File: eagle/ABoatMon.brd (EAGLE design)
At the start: 78.7 x 61 mm, 29 parts, among them J1 5V, J2 GND, J3 GND, J4 5V, X1 MKDSN1,5/2-5,08

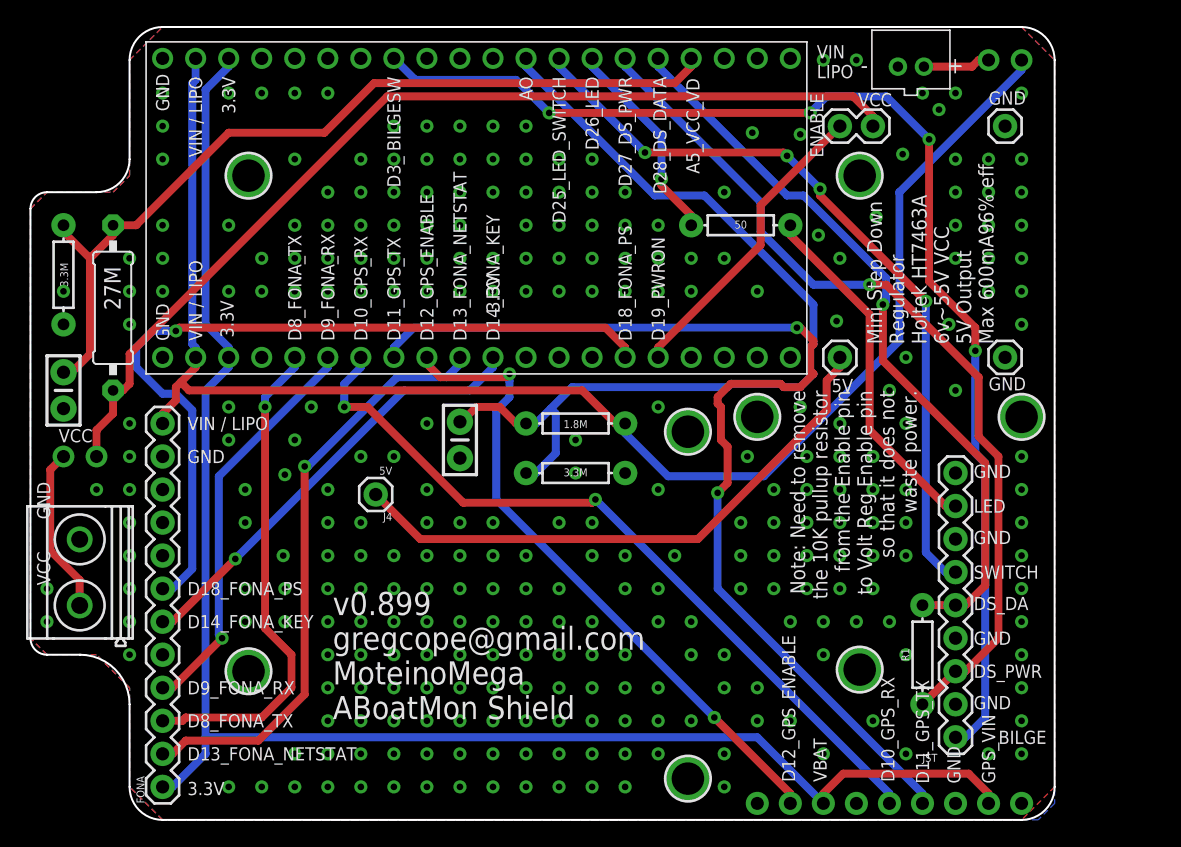
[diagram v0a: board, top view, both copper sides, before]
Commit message: moved 9 pin jst
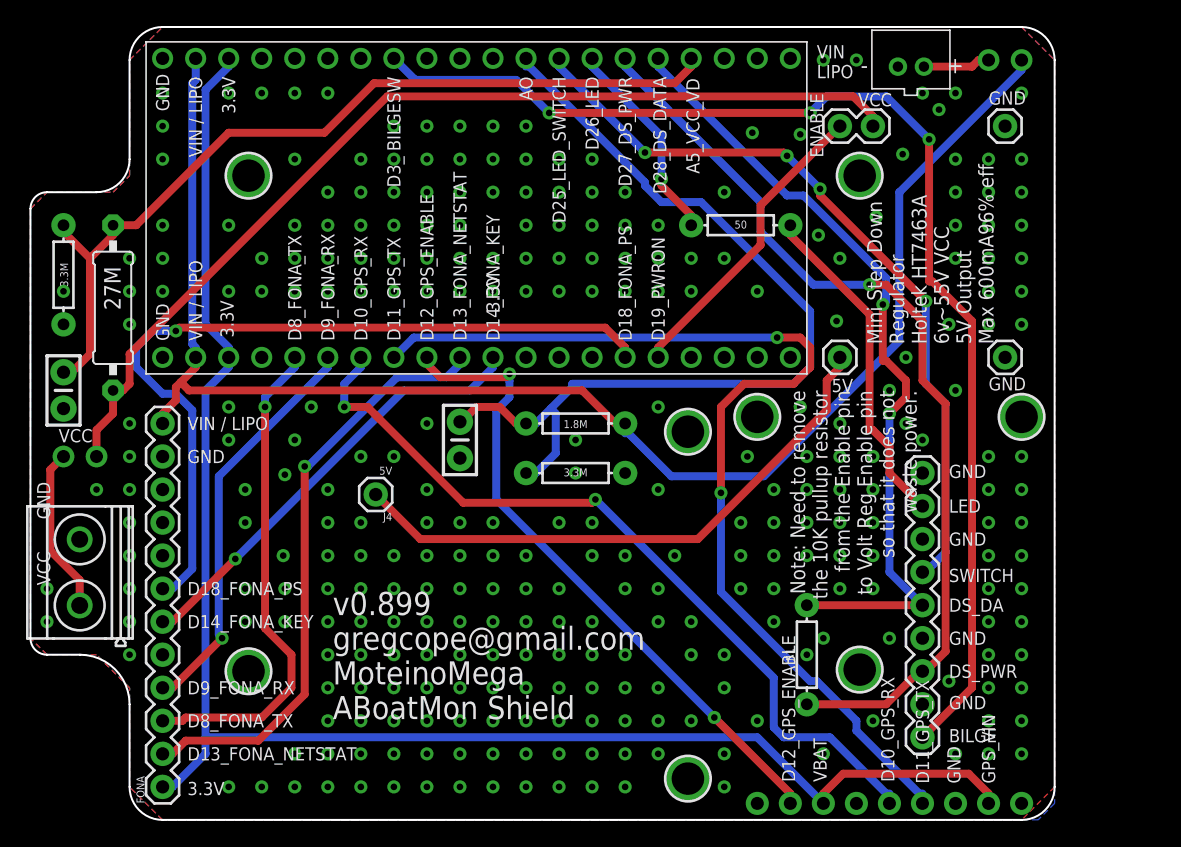
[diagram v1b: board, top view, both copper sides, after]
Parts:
- moved R1 8.89 mm to (61.0, 12.7)
- moved JST 2.54 mm to (69.8, 6.35)
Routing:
- net D28_DS_DATA: track 57.3 -> 61.5 mm, vias 1 -> 2
- net D27_DS_PWR: track 67.7 -> 71.4 mm
- net D11_GPS_TX: track 83.5 -> 80.5 mm
- net D10_GPS_RX: track 59.5 -> 62.3 mm
- net LED: track 27.3 -> 25.9 mm
- net A0: track 72.4 -> 71.6 mm
- net VIN: track 117.8 -> 118.4 mm
- net D3_BILGESW: track 93.9 -> 93.8 mm, vias 4 -> 3

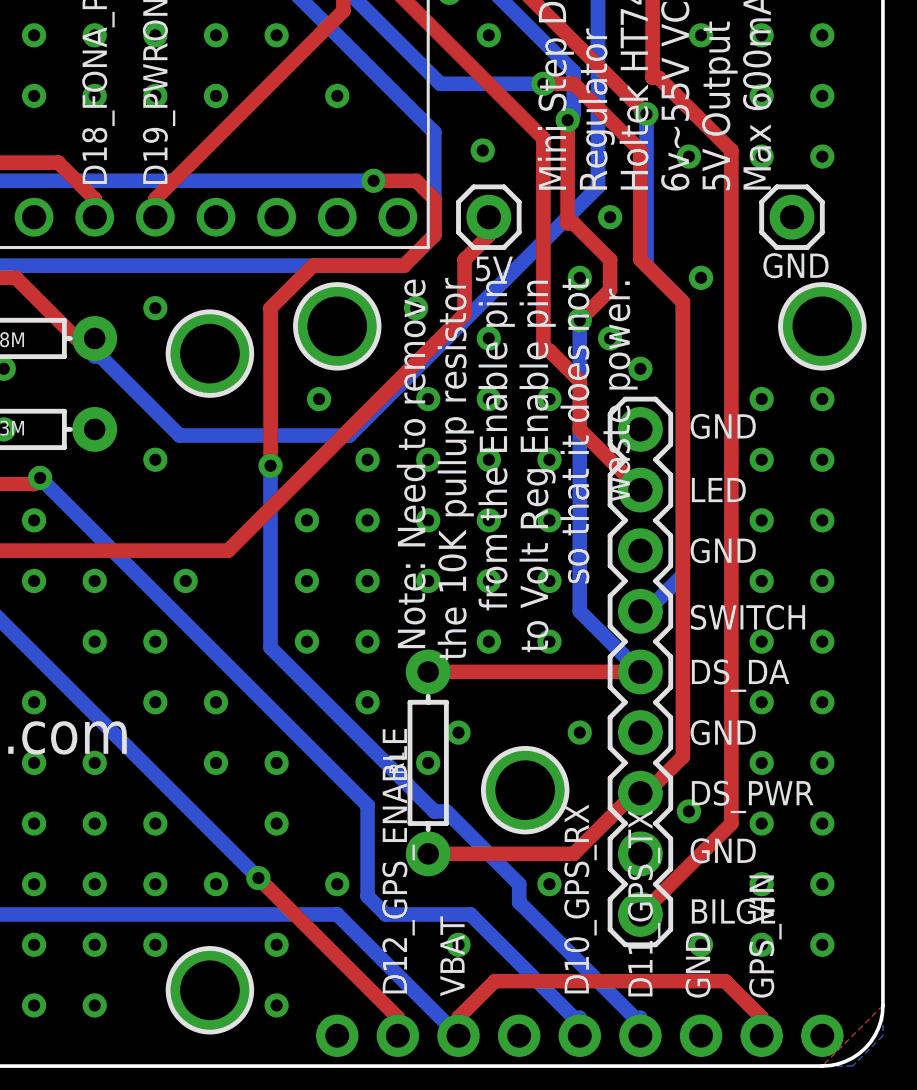
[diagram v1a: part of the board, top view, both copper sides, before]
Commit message: moved large JST
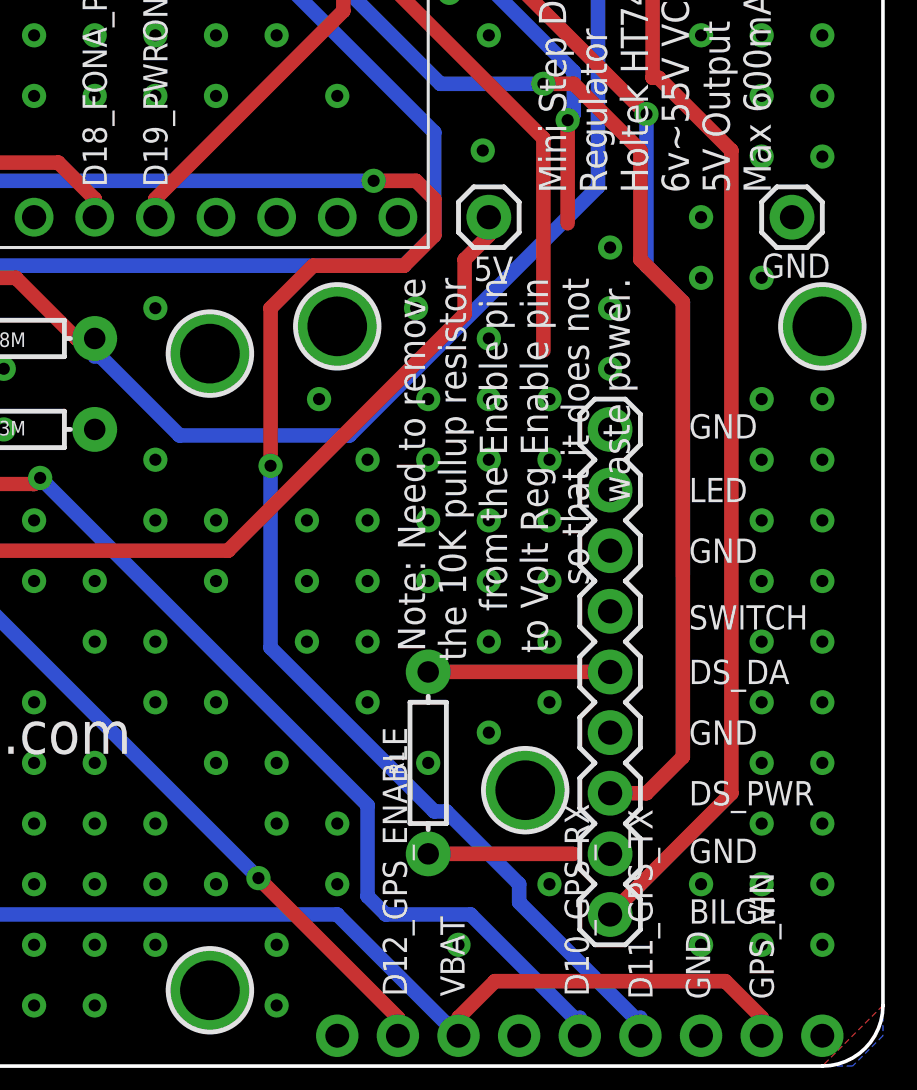
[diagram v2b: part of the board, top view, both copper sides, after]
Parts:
- moved JST 1.27 mm to (68.6, 6.35)
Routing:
- net D28_DS_DATA: track 61.5 -> 39.0 mm, vias 2 -> 1
- net LED: track 25.9 -> 18.3 mm
- net D27_DS_PWR: track 71.4 -> 68.8 mm
- net D25_LED_SWITCH: track 59.3 -> 56.9 mm
- net D3_BILGESW: track 93.8 -> 94.4 mm

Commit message: message logic
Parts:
- added J5: (no value), SparkFun-Connectors:JST-4-PTH
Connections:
- new net D16_SCL: J5.3, MOTEINO_MEGA.D16
- new net D17_SDA: J5.4, MOTEINO_MEGA.D17
- new net D20_OLED_VCC: J5.2, MOTEINO_MEGA.D20
- net GND: now also J5.1
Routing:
- net VCC_JUMPER: track 76.1 -> 48.1 mm
- net 3.3V: track 125.1 -> 100.7 mm
- net VIN: track 118.4 -> 96.3 mm
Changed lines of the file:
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@@
 <attribute name="VALUE" x="60.706" y="12.7" size="0.6096" layer="27" font="vector" ratio="20" rot="R90" align="top-center"/>
+</element>
+<element name="J5" library="SparkFun-Connectors" library_urn="urn:adsk.eagle:library:513" package="JST-4-PTH" package3d_urn="urn:adsk.eagle:package:38101/1" value="" x="15.24" y="43.18" smashed="yes" rot="R90">
+<attribute name="NAME" x="11.811" y="41.783" size="0.6096" layer="25" font="vector" ratio="20" rot="R90"/>
+<attribute name="PROD_ID" value="WIRE-13531" x="15.24" y="43.18" size="1.778" layer="27" rot="R90" display="off"/>
+<attribute name="SF_ID" value="PRT-09916" x="15.24" y="43.18" size="1.778" layer="27" rot="R90" display="off"/>
+<attribute name="VALUE" x="12.7" y="41.529" size="0.6096" layer="27" font="vector" ratio="20" rot="R90"/>
 </element>
 </elements>
@@
 <via x="29.21" y="43.18" extent="1-16" drill="0.508"/>
 <via x="31.75" y="43.18" extent="1-16" drill="0.508"/>
-<via x="16.51" y="40.64" extent="1-16" drill="0.508"/>
 <via x="19.05" y="40.64" extent="1-16" drill="0.508"/>
 <via x="21.59" y="40.64" extent="1-16" drill="0.508"/>
@@
 <via x="8.89" y="15.24" extent="1-16" drill="0.508"/>
 <via x="2.54" y="15.24" extent="1-16" drill="0.508"/>
-<via x="16.51" y="45.72" extent="1-16" drill="0.508"/>
 <via x="21.59" y="50.8" extent="1-16" drill="0.508"/>
 <via x="77.47" y="38.1" extent="1-16" drill="0.508"/>
@@
 <via x="72.39" y="33.02" extent="1-16" drill="0.508"/>
 <via x="72.39" y="35.56" extent="1-16" drill="0.508"/>
+<contactref element="J5" pad="1"/>
 </signal>
 <signal name="VIN" class="1">
@@
 <wire x1="11.43" y1="31.242" x2="12.446" y2="32.258" width="0.6096" layer="1"/>
 <wire x1="11.43" y1="30.48" x2="11.43" y2="31.242" width="0.6096" layer="1"/>
-<wire x1="13.97" y1="56.896" x2="13.97" y2="58.547" width="0.6096" layer="16"/>
 <wire x1="13.716" y1="56.642" x2="13.97" y2="56.896" width="0.6096" layer="16"/>
-<wire x1="13.716" y1="36.576" x2="13.716" y2="56.642" width="0.6096" layer="16"/>
-<wire x1="13.97" y1="36.322" x2="13.716" y2="36.576" width="0.6096" layer="16"/>
 <wire x1="13.97" y1="35.56" x2="13.97" y2="36.322" width="0.6096" layer="16"/>
 <wire x1="77.47" y1="57.658" x2="77.47" y2="58.42" width="0.6096" layer="16"/>
@@
 <wire x1="47.244" y1="29.718" x2="50.546" y2="26.416" width="0.6096" layer="16"/>
 <wire x1="47.244" y1="29.718" x2="46.99" y2="30.48" width="0.6096" layer="16"/>
+<wire x1="13.97" y1="56.896" x2="13.97" y2="58.547" width="0" layer="19" extent="16-16"/>
+<wire x1="13.97" y1="36.322" x2="13.716" y2="56.642" width="0" layer="19" extent="16-16"/>
 </signal>
 <signal name="A0">
@@
 <wire x1="74.93" y1="2.032" x2="73.406" y2="3.556" width="0.6096" layer="1"/>
 <wire x1="74.93" y1="1.27" x2="74.93" y2="2.032" width="0.6096" layer="1"/>
-<wire x1="16.51" y1="36.322" x2="16.51" y2="35.56" width="0.6096" layer="16"/>
-<wire x1="14.732" y1="38.1" x2="16.51" y2="36.322" width="0.6096" layer="16"/>
-<wire x1="14.732" y1="56.134" x2="14.732" y2="38.1" width="0.6096" layer="16"/>
-<wire x1="16.51" y1="57.912" x2="14.732" y2="56.134" width="0.6096" layer="16"/>
-<wire x1="16.51" y1="58.547" x2="16.51" y2="57.912" width="0.6096" layer="16"/>
 <wire x1="12.192" y1="2.54" x2="11.43" y2="2.54" width="0.6096" layer="16"/>
 <wire x1="14.732" y1="5.08" x2="12.192" y2="2.54" width="0.6096" layer="16"/>
@@
 <wire x1="57.15" y1="6.35" x2="62.23" y2="1.27" width="0.6096" layer="16"/>
 <wire x1="14.732" y1="6.35" x2="57.15" y2="6.35" width="0.6096" layer="16"/>
+<wire x1="16.51" y1="35.56" x2="16.51" y2="58.547" width="0" layer="19" extent="1-1"/>
 </signal>
 <signal name="D9_FONA_RX">
@@
 <wire x1="64.516" y1="55.626" x2="66.04" y2="54.102" width="0.6096" layer="1"/>
 <wire x1="28.702" y1="55.626" x2="64.516" y2="55.626" width="0.6096" layer="1"/>
-<wire x1="8.89" y1="35.814" x2="28.702" y2="55.626" width="0.6096" layer="1"/>
 <wire x1="8.89" y1="33.528" x2="8.89" y2="35.814" width="0.6096" layer="1"/>
 <wire x1="8.382" y1="33.02" x2="8.89" y2="33.528" width="0.6096" layer="1"/>
 <wire x1="8.382" y1="33.02" x2="7.62" y2="33.02" width="0.6096" layer="1"/>
+<wire x1="8.89" y1="35.814" x2="28.702" y2="55.626" width="0" layer="19" extent="1-1"/>
 </signal>
 <signal name="VIN_JUMPER" class="1">
@@
 <signal name="3.3V1" class="1">
 </signal>
+<signal name="D17_SDA">
+<contactref element="MOTEINO_MEGA" pad="D17"/>
+<contactref element="J5" pad="4"/>
+<wire x1="15.24" y1="46.18" x2="44.45" y2="35.56" width="0" layer="19" extent="1-1"/>
+</signal>
+<signal name="D16_SCL">
+<contactref element="MOTEINO_MEGA" pad="D16"/>
+<contactref element="J5" pad="3"/>
+<wire x1="15.24" y1="44.18" x2="41.91" y2="35.56" width="0" layer="19" extent="1-1"/>
+</signal>
+<signal name="D20_OLED_VCC">
+<contactref element="MOTEINO_MEGA" pad="D20"/>
+<contactref element="J5" pad="2"/>
+<wire x1="15.24" y1="42.18" x2="52.07" y2="35.56" width="0" layer="19" extent="1-1"/>
+</signal>
 </signals>

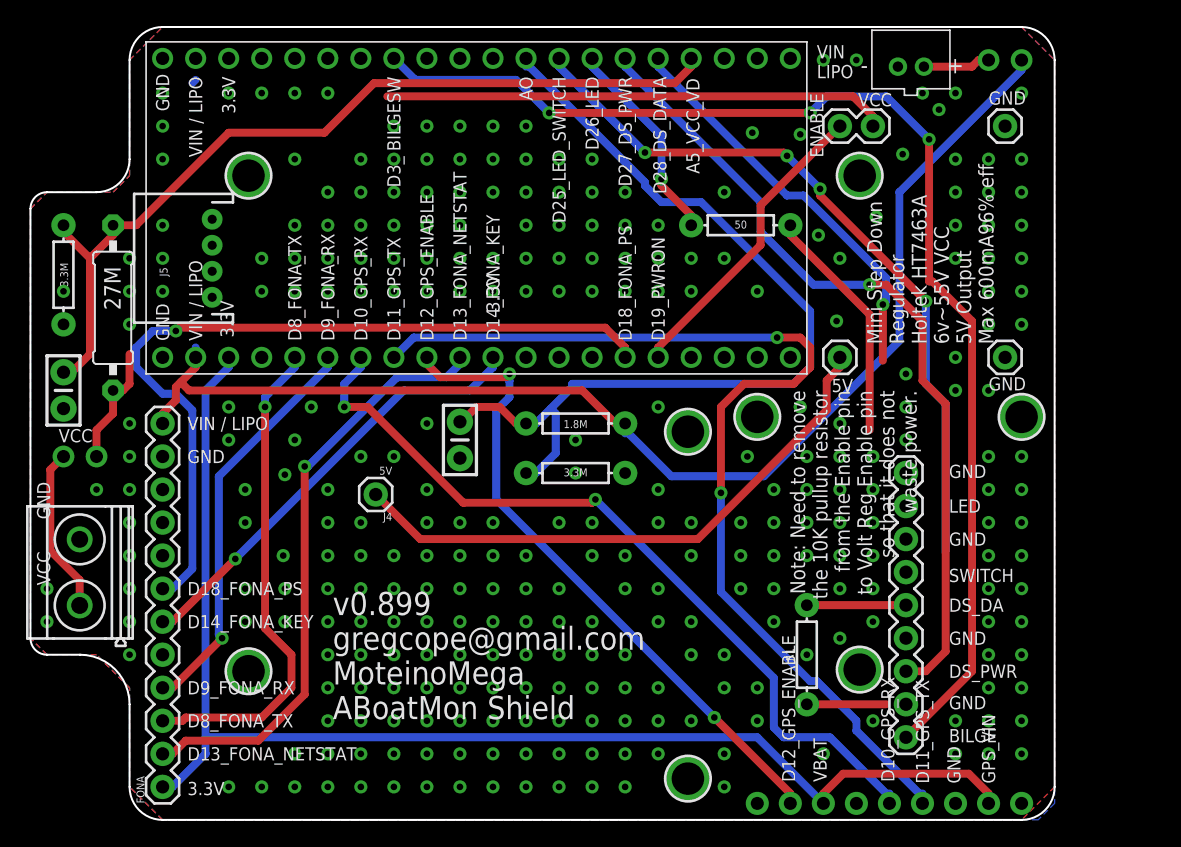
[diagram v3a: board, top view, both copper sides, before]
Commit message: eagle jst added
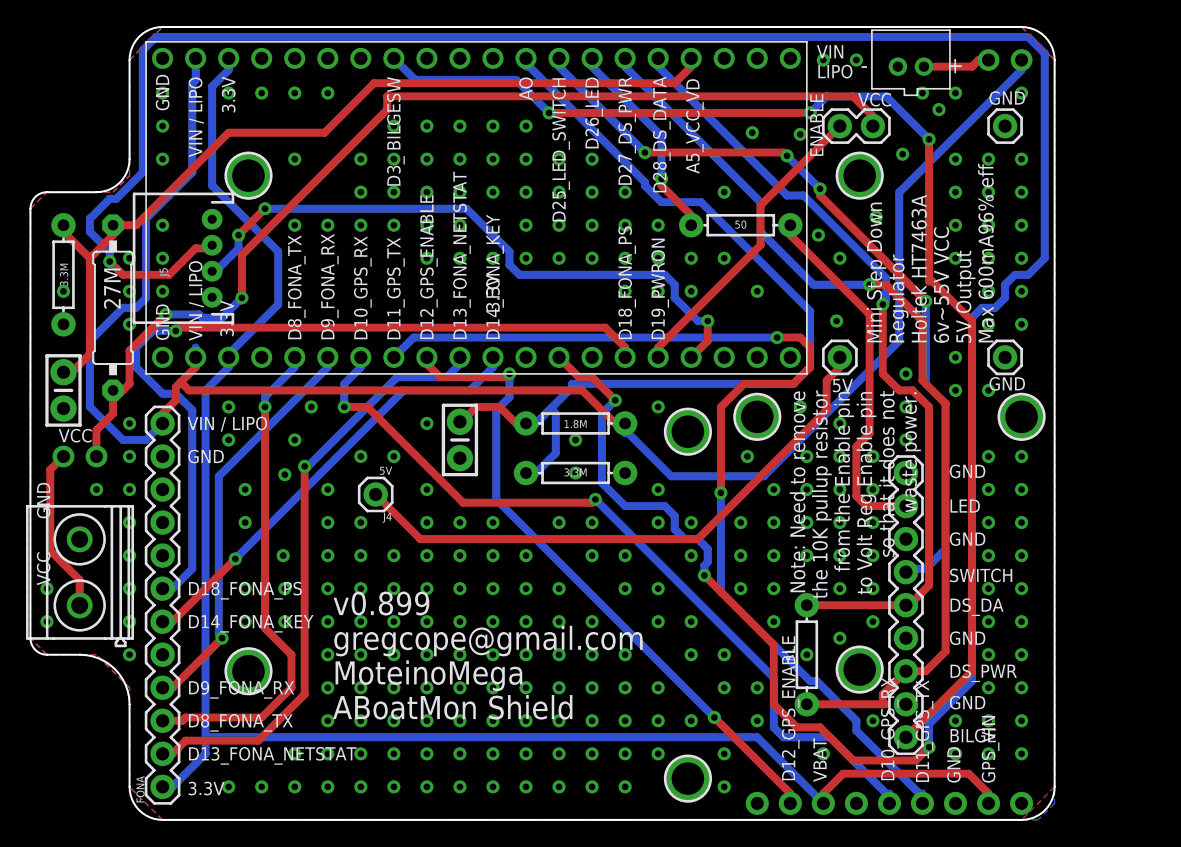
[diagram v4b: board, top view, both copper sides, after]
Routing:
- net D16_SCL: track 0.00 -> 208.4 mm, vias 0 -> 4
- net D20_OLED_VCC: track 0.00 -> 48.9 mm, vias 0 -> 3
- net VIN: track 96.3 -> 133.9 mm
- net VCC_JUMPER: track 48.1 -> 79.0 mm, vias 0 -> 2
- net 3.3V: track 100.7 -> 127.9 mm
- net D28_DS_DATA: track 39.0 -> 60.7 mm
- net LED: track 18.3 -> 27.9 mm
- net D25_LED_SWITCH: track 56.9 -> 60.5 mm
- net D27_DS_PWR: track 68.8 -> 72.1 mm

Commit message: added JST - drc issues still
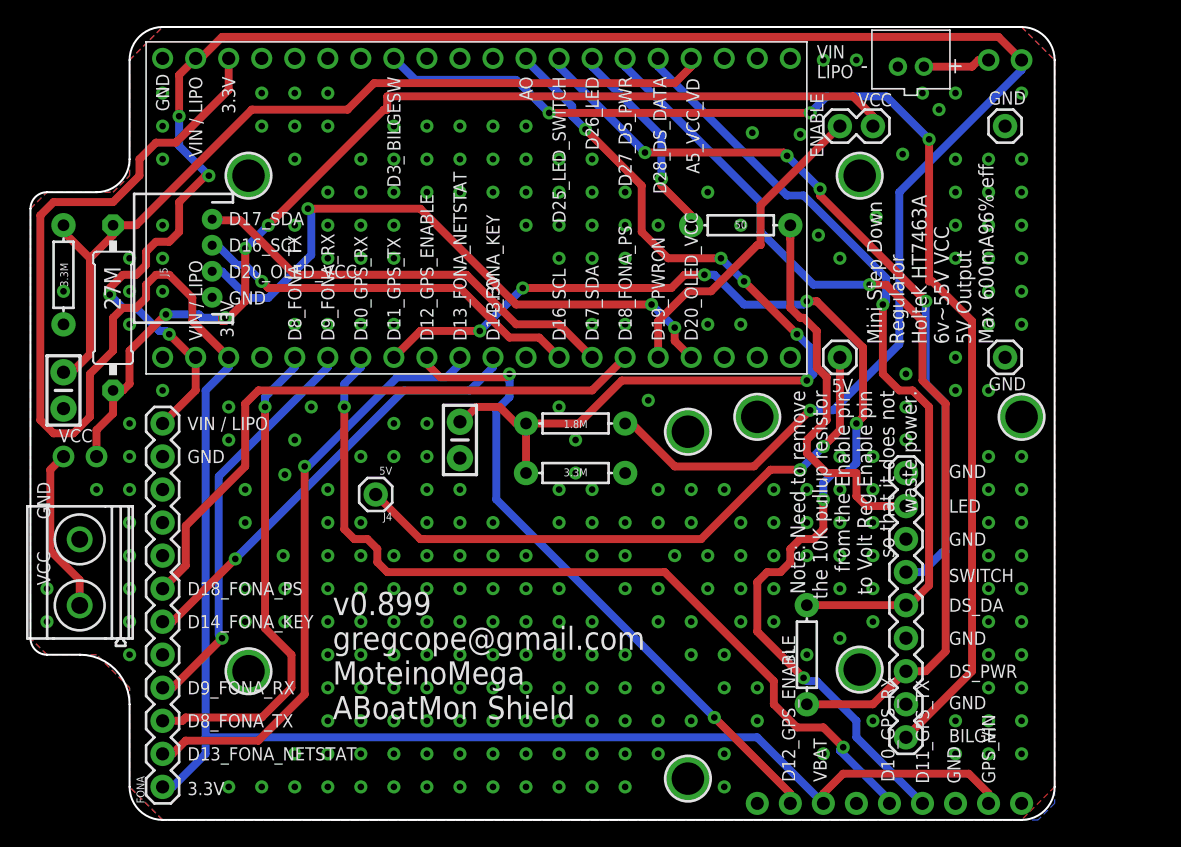
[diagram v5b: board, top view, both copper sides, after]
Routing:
- net D16_SCL: track 208.4 -> 30.3 mm, vias 4 -> 1
- net 3.3V: track 127.9 -> 165.7 mm
- net D17_SDA: track 0.00 -> 33.7 mm
- net VIN: track 133.9 -> 155.9 mm, vias 0 -> 5
- net D18_FONA_PS: track 61.9 -> 47.5 mm, vias 1 -> 0
- net D11_GPS_TX: track 80.5 -> 87.1 mm, vias 2 -> 7
- net D10_GPS_RX: track 62.3 -> 66.7 mm
- net A0: track 71.6 -> 69.4 mm, vias 0 -> 5
- net LED: track 27.9 -> 29.8 mm
- net 5V: track 44.7 -> 46.2 mm, vias 0 -> 2
- net VCC_JUMPER: track 79.0 -> 80.3 mm, vias 2 -> 4
- net D19_PWRON: track 23.6 -> 24.8 mm
- net D27_DS_PWR: track 72.1 -> 71.4 mm
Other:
- board text added: "D16_SCL"
- board text added: "D17_SDA"
- board text added: "D20_OLED_VCC"
